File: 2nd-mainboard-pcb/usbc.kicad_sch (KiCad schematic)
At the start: 13 parts, among them J1 USB_C_Receptacle, U2 PTS647SM38SMTR2LFS, U5 FT232RL

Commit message: verpolungsschutz und powerin
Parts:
- renumbered R1 to R21
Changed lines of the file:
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@@
 		(dnp no)
 		(fields_autoplaced yes)
-		(property "Reference" "R1"
+		(property "Reference" "R21"
 			(at 86.36 67.3099 0)
 			(effects
@@
 			(project "2nd-mainboard-pcb"
 				(path "/6926a609-8b92-4b3a-88c8-3d023174b977/c1b5568e-d56d-48b3-9b9c-ea1ab28283d3"
-					(reference "R1")
+					(reference "R21")
 					(unit 1)
 				)

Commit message: finished stacked design, annotaded
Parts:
- removed D1: SMAJ5.0A, Diode_SMD:D_SMA, symbol Diode:SMAJ5.0A
- added C15: 10µF, symbol Device:C
- added C16: 100nF, symbol Device:C
- added D2: WE-TVSP_DO-214AA_600W_BI, WE-TVSP_DO-214AA_600W_BI:WE-TVSP_DO-214AA_BIDIRECTIONAL, symbol Imported_Component_Symbols:WE-TVSP_DO-214AA_600W_BI
- U5: renamed from U2; footprint SW_PTS647SM38SMTR2LFS_CNK -> Imported_Component_Footprints:SW_PTS647SM38SMTR2LFS_CNK
- renumbered C1 to C14, C2 to C17, C4 to C18, D2 to D3, J1 to J2, R2 to R10, R3 to R11, R4 to R12, R5 to R13, R21 to R9, U5 to U6
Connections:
- net +5V: no longer C18.1, J2.A4 (VBUS), J2.A9 (VBUS), J2.B4 (VBUS), J2.B9 (VBUS), R11.1, U6.20 (VCC), U6.4 (VCCIO)
- net GND: now also U6.25 (AGND), C15.2, C16.2, D2.1
- new net +5V_POW: R11.1, U6.4 (VCCIO)
- new net +5V_USBC: C15.1, C16.1, C18.1, D2.2, J2.A4 (VBUS), J2.A9 (VBUS), J2.B4 (VBUS), J2.B9 (VBUS), U6.20 (VCC)
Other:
- moved on the sheet: C14, C17, C18, D3, J2, R10, R11, R12, R13, R9, U5, U6

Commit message: alle bauteile hinzugefügt
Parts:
- removed D3: LED, symbol Device:LED
- removed J2: USB_C_Receptacle, Connector_USB:USB_C_Receptacle_GCT_USB4085, symbol Connector:USB_C_Receptacle
- removed R12, R13: 10k, symbol Device:R
- added P1: USB_C_Plug_USB2.0, Connector_USB:USB_C_Receptacle_GCT_USB4085, symbol Connector:USB_C_Plug_USB2.0
- C15: footprint (none) -> Capacitor_SMD:C_0805_2012Metric_Pad1.18x1.45mm_HandSolder
- C16: footprint (none) -> Capacitor_SMD:C_0402_1005Metric_Pad0.74x0.62mm_HandSolder
- C17: renamed from C18; footprint (none) -> Capacitor_SMD:C_0402_1005Metric_Pad0.74x0.62mm_HandSolder
- C18: renamed from C17; footprint (none) -> Capacitor_SMD:C_0402_1005Metric_Pad0.74x0.62mm_HandSolder
- C19: renamed from C14; footprint (none) -> Capacitor_SMD:C_0805_2012Metric_Pad1.18x1.45mm_HandSolder
- D2: footprint WE-TVSP_DO-214AA_600W_BI:WE-TVSP_DO-214AA_BIDIRECTIONAL -> Imported_Component_Footprints:824521241
- R10, R11, R9: footprint (none) -> Resistor_SMD:R_0402_1005Metric
- renumbered U6 to U5, U5 to U6
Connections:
- net +5V_USBC: now also P1.A4 (VBUS), P1.A9 (VBUS), P1.B4 (VBUS), P1.B9 (VBUS)
- net GND: now also P1.A1 (GND), P1.A12 (GND), P1.B1 (GND), P1.B12 (GND)
- net USBD+: now also P1.A6 (D+)
- net USBD-: now also P1.A7 (D-)
- net at R9.1: now also P1.B5 (VCONN)
- net at C19.1: now also P1.S1 (SHIELD)
- net at R10.1: now also P1.A5 (CC)
- no-connect marks 23 -> 16
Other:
- moved on the sheet: C19

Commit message: mehr positioning
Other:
- moved on the sheet: C17, C18, R11, U5, U6

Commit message: Fan-PCB-Beginning
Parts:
- removed C18: 100nF, Capacitor_SMD:C_0402_1005Metric_Pad0.74x0.62mm_HandSolder, symbol Device:C
- renumbered C19 to C18
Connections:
- net +3V3: no longer names the net of U5.17 (3V3OUT)
- no-connect marks 16 -> 18
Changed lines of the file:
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@@
-	)
-	(junction
-		(at 132.08 62.23)
-		(diameter 0)
-		(color 0 0 0 0)
 	)
 	(junction
@@
 	)
 	(no_connect
+		(at 149.86 53.34)
+	)
+	(no_connect
+		(at 156.21 62.23)
+	)
+	(no_connect
 		(at 196.85 97.79)
 	)
@@
 	(wire
 		(pts
-			(xy 132.08 69.85) (xy 132.08 73.66)
-		)
-		(stroke
-			(width 0)
-			(type default)
-		)
-	)
-	(wire
-		(pts
 			(xy 57.15 20.32) (xy 64.77 20.32)
 		)
@@
 	(wire
 		(pts
-			(xy 132.08 62.23) (xy 156.21 62.23)
-		)
-		(stroke
-			(width 0)
-			(type default)
-		)
-	)
-	(wire
-		(pts
 			(xy 109.22 36.83) (xy 109.22 31.75)
 		)
@@
 		(pts
 			(xy 152.4 80.01) (xy 156.21 80.01)
-		)
-		(stroke
-			(width 0)
-			(type default)
-		)
-	)
-	(wire
-		(pts
-			(xy 132.08 59.69) (xy 132.08 62.23)
 		)
 		(stroke
@@
 		(dnp no)
 		(fields_autoplaced yes)
-		(property "Reference" "#PWR026"
+		(property "Reference" "#PWR027"
 			(at 62.23 63.5 0)
 			(effects
@@
 			(project "2nd-mainboard-pcb"
 				(path "/6926a609-8b92-4b3a-88c8-3d023174b977/c1b5568e-d56d-48b3-9b9c-ea1ab28283d3"
-					(reference "#PWR026")
+					(reference "#PWR027")
 					(unit 1)
 				)
@@
 		(dnp no)
 		(fields_autoplaced yes)
-		(property "Reference" "#PWR024"
+		(property "Reference" "#PWR023"
 			(at 179.07 39.37 0)
 			(effects
@@
 			(project "2nd-mainboard-pcb"
 				(path "/6926a609-8b92-4b3a-88c8-3d023174b977/c1b5568e-d56d-48b3-9b9c-ea1ab28283d3"
-					(reference "#PWR024")
+					(reference "#PWR023")
 					(unit 1)
 				)
@@
 		(dnp no)
 		(fields_autoplaced yes)
-		(property "Reference" "C19"
+		(property "Reference" "C18"
 			(at 26.67 78.7399 0)
 			(effects
@@
 			(project "2nd-mainboard-pcb"
 				(path "/6926a609-8b92-4b3a-88c8-3d023174b977/c1b5568e-d56d-48b3-9b9c-ea1ab28283d3"
-					(reference "C19")
+					(reference "C18")
 					(unit 1)
 				)
@@
 		(dnp no)
 		(fields_autoplaced yes)
-		(property "Reference" "#PWR027"
+		(property "Reference" "#PWR028"
 			(at 71.12 63.5 0)
 			(effects
@@
 			(project "2nd-mainboard-pcb"
 				(path "/6926a609-8b92-4b3a-88c8-3d023174b977/c1b5568e-d56d-48b3-9b9c-ea1ab28283d3"
-					(reference "#PWR027")
+					(reference "#PWR028")
 					(unit 1)
 				)
@@
 		(dnp no)
 		(fields_autoplaced yes)
-		(property "Reference" "#PWR035"
+		(property "Reference" "#PWR033"
 			(at 50.8 125.73 0)
 			(effects
@@
 			(project "2nd-mainboard-pcb"
 				(path "/6926a609-8b92-4b3a-88c8-3d023174b977/c1b5568e-d56d-48b3-9b9c-ea1ab28283d3"
-					(reference "#PWR035")
-					(unit 1)
-				)
-			)
-		)
-	)
-	(symbol
-		(lib_id "power:GND")
-		(at 132.08 73.66 0)
-		(unit 1)
-		(exclude_from_sim no)
-		(in_bom yes)
-		(on_board yes)
-		(dnp no)
-		(fields_autoplaced yes)
-		(property "Reference" "#PWR031"
-			(at 132.08 80.01 0)
-			(effects
-				(font
-					(size 1.27 1.27)
-				)
-				(hide yes)
-			)
-		)
-		(property "Value" "GND"
-			(at 132.08 78.74 0)
-			(effects
-				(font
-					(size 1.27 1.27)
-				)
-			)
-		)
-		(property "Footprint" ""
-			(at 132.08 73.66 0)
-			(effects
-				(font
-					(size 1.27 1.27)
-				)
-				(hide yes)
-			)
-		)
-		(property "Datasheet" ""
-			(at 132.08 73.66 0)
-			(effects
-				(font
-					(size 1.27 1.27)
-				)
-				(hide yes)
-			)
-		)
-		(property "Description" "Power symbol creates a global label with name \"GND\" , ground"
-			(at 132.08 73.66 0)
-			(effects
-				(font
-					(size 1.27 1.27)
-				)
-				(hide yes)
-			)
-		)
-		(pin "1"
-		)
-		(instances
-			(project "2nd-mainboard-pcb"
-				(path "/6926a609-8b92-4b3a-88c8-3d023174b977/c1b5568e-d56d-48b3-9b9c-ea1ab28283d3"
-					(reference "#PWR031")
+					(reference "#PWR033")
 					(unit 1)
 				)
@@
 		(on_board yes)
 		(dnp no)
-		(property "Reference" "#PWR034"
+		(property "Reference" "#PWR031"
 			(at 114.3 106.68 0)
 			(effects
@@
 			(project "2nd-mainboard-pcb"
 				(path "/6926a609-8b92-4b3a-88c8-3d023174b977/c1b5568e-d56d-48b3-9b9c-ea1ab28283d3"
-					(reference "#PWR034")
+					(reference "#PWR031")
 					(unit 1)
 				)
@@
 	)
 	(symbol
-		(lib_id "Device:C")
-		(at 132.08 66.04 0)
-		(unit 1)
-		(exclude_from_sim no)
-		(in_bom yes)
-		(on_board yes)
-		(dnp no)
-		(fields_autoplaced yes)
-		(property "Reference" "C18"
-			(at 135.89 64.7699 0)
-			(effects
-				(font
-					(size 1.27 1.27)
-				)
-				(justify left)
-			)
-		)
-		(property "Value" "100nF"
-			(at 135.89 67.3099 0)
-			(effects
-				(font
-					(size 1.27 1.27)
-				)
-				(justify left)
-			)
-		)
-		(property "Footprint" "Capacitor_SMD:C_0402_1005Metric_Pad0.74x0.62mm_HandSolder"
-			(at 133.0452 69.85 0)
-			(effects
-				(font
-					(size 1.27 1.27)
-				)
-				(hide yes)
-			)
-		)
-		(property "Datasheet" "~"
-			(at 132.08 66.04 0)
-			(effects
-				(font
-					(size 1.27 1.27)
-				)
-				(hide yes)
-			)
-		)
-		(property "Description" "Unpolarized capacitor"
-			(at 132.08 66.04 0)
-			(effects
-				(font
-					(size 1.27 1.27)
-				)
-				(hide yes)
-			)
-		)
-		(pin "1"
-		)
-		(pin "2"
-		)
-		(instances
-			(project "2nd-mainboard-pcb"
-				(path "/6926a609-8b92-4b3a-88c8-3d023174b977/c1b5568e-d56d-48b3-9b9c-ea1ab28283d3"
-					(reference "C18")
-					(unit 1)
-				)
-			)
-		)
-	)
-	(symbol
 		(lib_id "power:GND")
 		(at 193.04 50.8 0)
@@
 		(dnp no)
 		(fields_autoplaced yes)
-		(property "Reference" "#PWR028"
+		(property "Reference" "#PWR026"
 			(at 193.04 57.15 0)
 			(effects
@@
 			(project "2nd-mainboard-pcb"
 				(path "/6926a609-8b92-4b3a-88c8-3d023174b977/c1b5568e-d56d-48b3-9b9c-ea1ab28283d3"
-					(reference "#PWR028")
+					(reference "#PWR026")
 					(unit 1)
 				)
@@
 		(dnp no)
 		(fields_autoplaced yes)
-		(property "Reference" "#PWR030"
+		(property "Reference" "#PWR029"
 			(at 30.48 87.63 0)
 			(effects
@@
 			(project "2nd-mainboard-pcb"
 				(path "/6926a609-8b92-4b3a-88c8-3d023174b977/c1b5568e-d56d-48b3-9b9c-ea1ab28283d3"
-					(reference "#PWR030")
+					(reference "#PWR029")
 					(unit 1)
 				)
@@
 		(dnp no)
 		(fields_autoplaced yes)
-		(property "Reference" "#PWR032"
+		(property "Reference" "#PWR030"
 			(at 22.86 95.25 0)
 			(effects
@@
 			(project "2nd-mainboard-pcb"
 				(path "/6926a609-8b92-4b3a-88c8-3d023174b977/c1b5568e-d56d-48b3-9b9c-ea1ab28283d3"
-					(reference "#PWR032")
+					(reference "#PWR030")
 					(unit 1)
 				)
@@
 		(dnp no)
 		(fields_autoplaced yes)
-		(property "Reference" "#PWR033"
+		(property "Reference" "#PWR032"
 			(at 181.61 116.84 0)
 			(effects
@@
 			(project "2nd-mainboard-pcb"
 				(path "/6926a609-8b92-4b3a-88c8-3d023174b977/c1b5568e-d56d-48b3-9b9c-ea1ab28283d3"
-					(reference "#PWR033")
+					(reference "#PWR032")
 					(unit 1)
 				)
@@
 	)
 	(symbol
-		(lib_id "power:+3V3")
-		(at 132.08 59.69 0)
-		(unit 1)
-		(exclude_from_sim no)
-		(in_bom yes)
-		(on_board yes)
-		(dnp no)
-		(fields_autoplaced yes)
-		(property "Reference" "#PWR029"
-			(at 132.08 63.5 0)
-			(effects
-				(font
-					(size 1.27 1.27)
-				)
-				(hide yes)
-			)
-		)
-		(property "Value" "+3V3"
-			(at 132.08 54.61 0)
-			(effects
-				(font
-					(size 1.27 1.27)
-				)
-			)
-		)
-		(property "Footprint" ""
-			(at 132.08 59.69 0)
-			(effects
-				(font
-					(size 1.27 1.27)
-				)
-				(hide yes)
-			)
-		)
-		(property "Datasheet" ""
-			(at 132.08 59.69 0)
-			(effects
-				(font
-					(size 1.27 1.27)
-				)
-				(hide yes)
-			)
-		)
-		(property "Description" "Power symbol creates a global label with name \"+3V3\""
-			(at 132.08 59.69 0)
-			(effects
-				(font
-					(size 1.27 1.27)
-				)
-				(hide yes)
-			)
-		)
-		(pin "1"
-		)
-		(instances
-			(project "2nd-mainboard-pcb"
-				(path "/6926a609-8b92-4b3a-88c8-3d023174b977/c1b5568e-d56d-48b3-9b9c-ea1ab28283d3"
-					(reference "#PWR029")
-					(unit 1)
-				)
-			)
-		)
-	)
-	(symbol
 		(lib_id "power:GND")
 		(at 95.25 40.64 0)
@@
 		(dnp no)
 		(fields_autoplaced yes)
-		(property "Reference" "#PWR023"
+		(property "Reference" "#PWR024"
 			(at 95.25 46.99 0)
 			(effects
@@
 			(project "2nd-mainboard-pcb"
 				(path "/6926a609-8b92-4b3a-88c8-3d023174b977/c1b5568e-d56d-48b3-9b9c-ea1ab28283d3"
-					(reference "#PWR023")
+					(reference "#PWR024")
 					(unit 1)
 				)

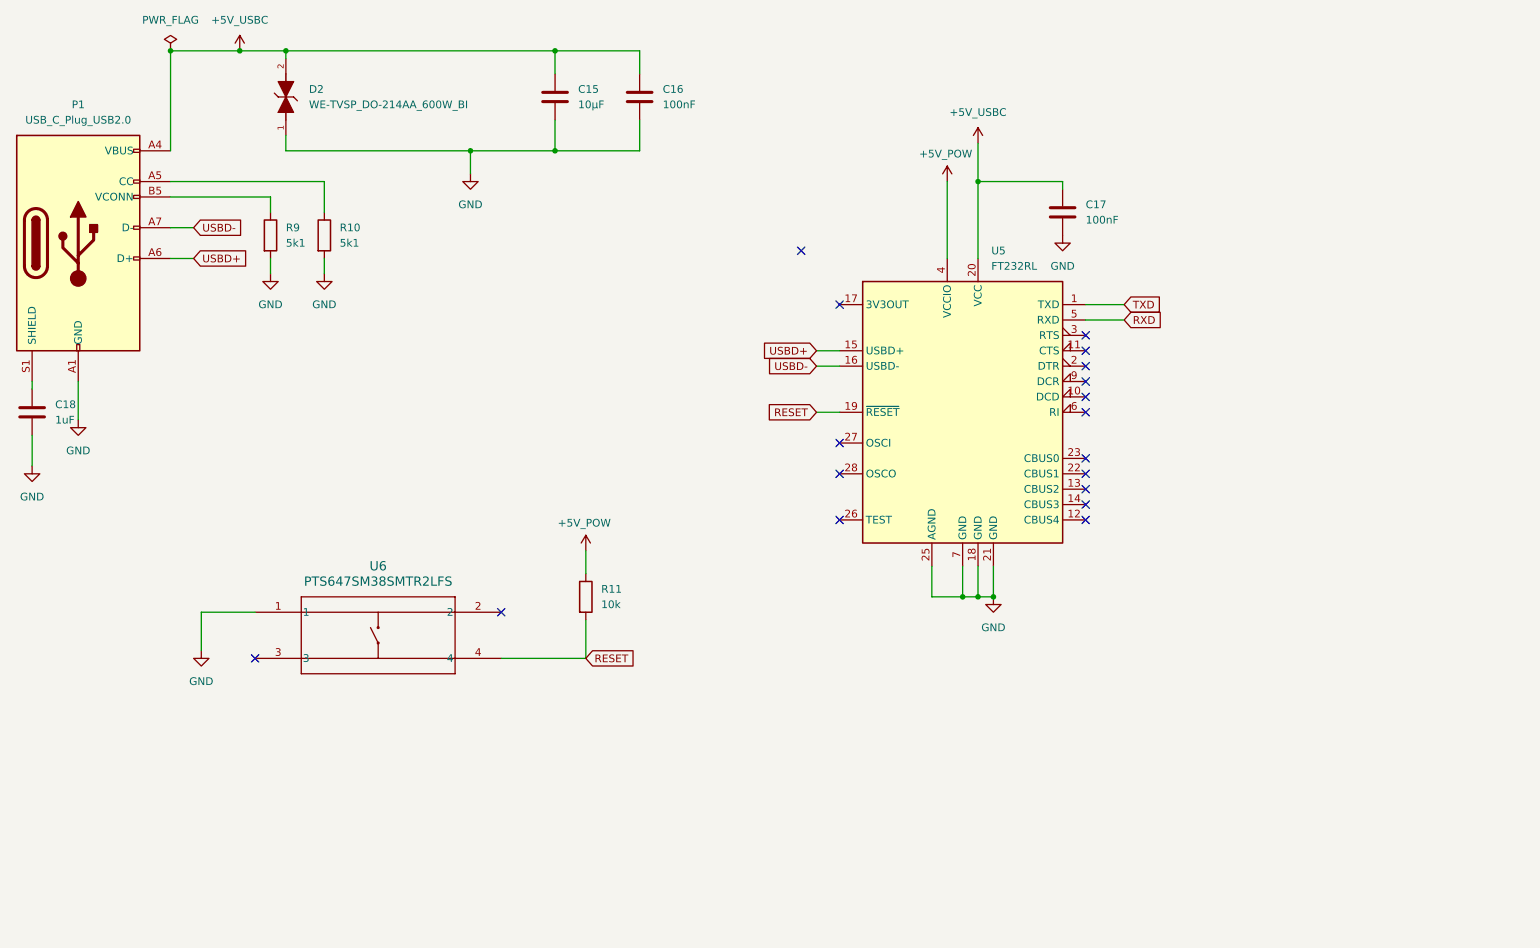
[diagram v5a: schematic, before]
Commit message: updated a bit of the track widths, removed comments in schematic
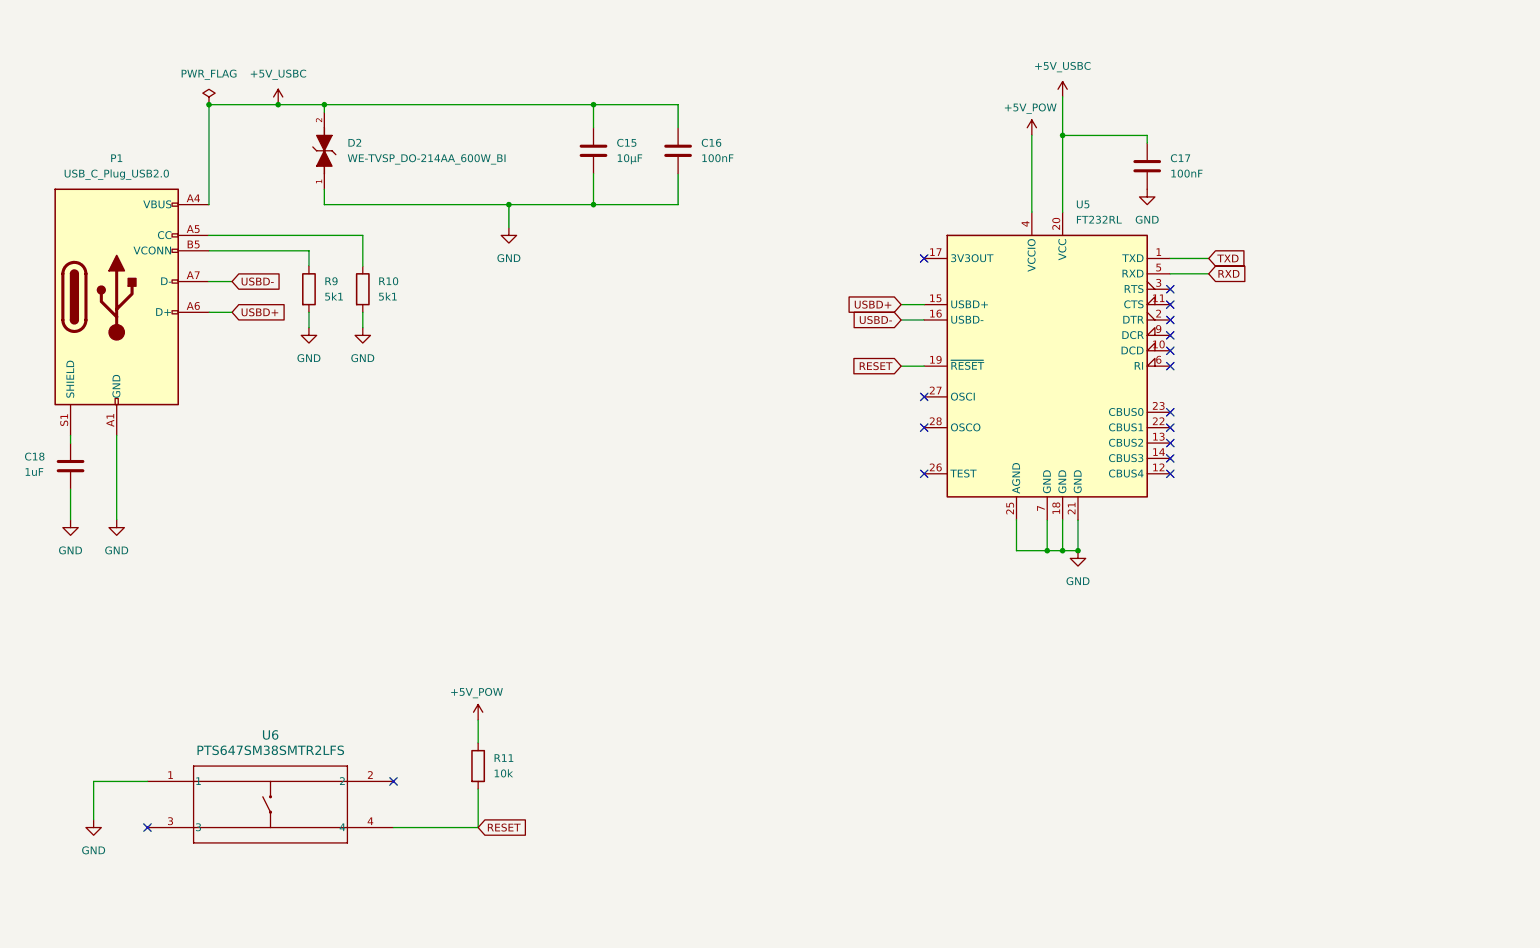
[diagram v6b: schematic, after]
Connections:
- no-connect marks 18 -> 17
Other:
- moved on the sheet: C15, C16, C17, C18, D2, P1, R10, R11, R9, U5, U6

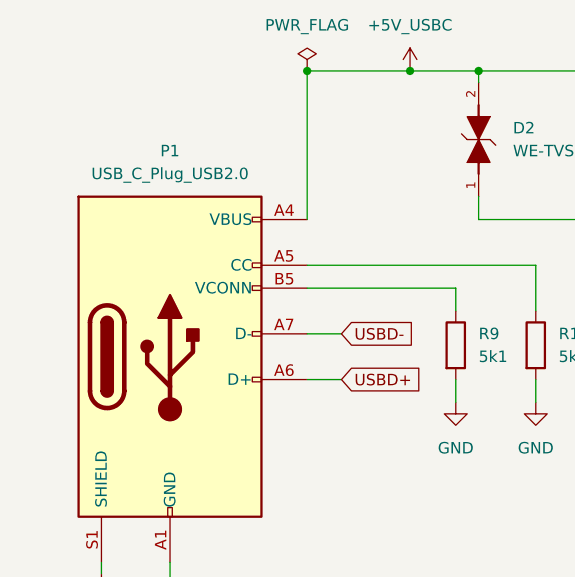
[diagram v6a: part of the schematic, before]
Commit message: further configured wireviz, editet excel
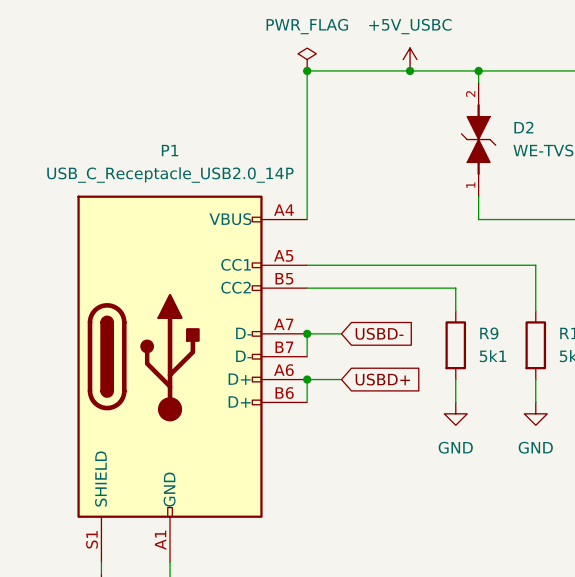
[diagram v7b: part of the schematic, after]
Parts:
- removed P1: USB_C_Plug_USB2.0, Connector_USB:USB_C_Receptacle_GCT_USB4085, symbol Connector:USB_C_Plug_USB2.0
- added P1: USB_C_Receptacle_USB2.0_14P, Connector_USB:USB_C_Receptacle_GCT_USB4085, symbol Connector:USB_C_Receptacle_USB2.0_14P
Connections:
- net +5V_USBC: now also P1.A4 (VBUS), P1.A9 (VBUS), P1.B4 (VBUS), P1.B9 (VBUS)
- net GND: now also P1.A1 (GND), P1.A12 (GND), P1.B1 (GND), P1.B12 (GND)
- net USBD+: now also P1.A6 (D+), P1.B6 (D+)
- net USBD-: now also P1.A7 (D-), P1.B7 (D-)
- net at R10.1: now also P1.A5 (CC1)
- net at R9.1: now also P1.B5 (CC2)
- net at C18.1: now also P1.S1 (SHIELD)
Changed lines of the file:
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@@
+	)
+	(junction
+		(at 52.07 58.42)
+		(diameter 0)
+		(color 0 0 0 0)
 	)
 	(junction
@@
 	)
 	(junction
+		(at 52.07 63.5)
+		(diameter 0)
+		(color 0 0 0 0)
+	)
+	(junction
 		(at 71.12 29.21)
 		(diameter 0)
@@
 	(wire
 		(pts
+			(xy 52.07 63.5) (xy 52.07 66.04)
+		)
+		(stroke
+			(width 0)
+			(type default)
+		)
+	)
+	(wire
+		(pts
 			(xy 96.52 130.81) (xy 96.52 134.62)
 		)
@@
 		(pts
 			(xy 129.54 40.64) (xy 129.54 45.72)
+		)
+		(stroke
+			(width 0)
+			(type default)
+		)
+	)
+	(wire
+		(pts
+			(xy 52.07 58.42) (xy 52.07 60.96)
 		)
 		(stroke
@@
 	)
 	(symbol
-		(lib_id "Connector:USB_C_Plug_USB2.0")
-		(at 36.83 60.96 0)
-		(unit 1)
-		(exclude_from_sim no)
-		(in_bom yes)
-		(on_board yes)
-		(dnp no)
-		(fields_autoplaced yes)
-		(property "Reference" "P1"
-			(at 36.83 38.1 0)
-			(effects
-				(font
-					(size 1.27 1.27)
-				)
-			)
-		)
-		(property "Value" "USB_C_Plug_USB2.0"
-			(at 36.83 40.64 0)
-			(effects
-				(font
-					(size 1.27 1.27)
-				)
-			)
-		)
-		(property "Footprint" "Connector_USB:USB_C_Receptacle_GCT_USB4085"
-			(at 40.64 60.96 0)
-			(effects
-				(font
-					(size 1.27 1.27)
-				)
-				(hide yes)
-			)
-		)
-		(property "Datasheet" "https://www.usb.org/sites/default/files/documents/usb_type-c.zip"
-			(at 40.64 60.96 0)
-			(effects
-				(font
-					(size 1.27 1.27)
-				)
-				(hide yes)
-			)
-		)
-		(property "Description" "USB 2.0-only Type-C Plug connector"
-			(at 36.83 60.96 0)
-			(effects
-				(font
-					(size 1.27 1.27)
-				)
-				(hide yes)
-			)
-		)
-		(pin "B5"
-		)
-		(pin "B9"
-		)
-		(pin "A9"
-		)
-		(pin "B12"
-		)
-		(pin "B1"
-		)
-		(pin "A12"
-		)
-		(pin "A5"
-		)
-		(pin "A4"
-		)
-		(pin "A1"
-		)
-		(pin "B4"
-		)
-		(pin "A7"
-		)
-		(pin "S1"
-		)
-		(pin "A6"
-		)
-		(instances
-			(project ""
-				(path "/6926a609-8b92-4b3a-88c8-3d023174b977/c1b5568e-d56d-48b3-9b9c-ea1ab28283d3"
-					(reference "P1")
-					(unit 1)
-				)
-			)
-		)
-	)
-	(symbol
 		(lib_id "Device:C")
 		(at 207.01 39.37 0)
@@
 					(unit 1)
 				)
+			)
+		)
+	)
+	(symbol
+		(lib_id "Connector:USB_C_Receptacle_USB2.0_14P")
+		(at 36.83 60.96 0)
+		(unit 1)
+		(exclude_from_sim no)
+		(in_bom yes)
+		(on_board yes)
+		(dnp no)
+		(fields_autoplaced yes)
+		(property "Reference" "P1"
+			(at 36.83 38.1 0)
+			(effects
+				(font
+					(size 1.27 1.27)
+				)
+			)
+		)
+		(property "Value" "USB_C_Receptacle_USB2.0_14P"
+			(at 36.83 40.64 0)
+			(effects
+				(font
+					(size 1.27 1.27)
+				)
+			)
+		)
+		(property "Footprint" "Connector_USB:USB_C_Receptacle_GCT_USB4085"
+			(at 40.64 60.96 0)
+			(effects
+				(font
+					(size 1.27 1.27)
+				)
+				(hide yes)
+			)
+		)
+		(property "Datasheet" "https://www.usb.org/sites/default/files/documents/usb_type-c.zip"
+			(at 40.64 60.96 0)
+			(effects
+				(font
+					(size 1.27 1.27)
+				)
+				(hide yes)
+			)
+		)
+		(property "Description" "USB 2.0-only 14P Type-C Receptacle connector"
+			(at 36.83 60.96 0)
+			(effects
+				(font
+					(size 1.27 1.27)
+				)
+				(hide yes)
+			)
+		)
+		(pin "A5"
+		)
+		(pin "B5"
+		)
+		(pin "A4"
+		)
+		(pin "B9"
+		)
+		(pin "B7"
+		)
+		(pin "S1"
+		)
+		(pin "B6"
+		)
+		(pin "B12"
+		)
+		(pin "A12"
+		)
+		(pin "A6"
+		)
+		(pin "B4"
+		)
+		(pin "A7"
+		)
+		(pin "A9"
+		)
+		(pin "B1"
+		)
+		(pin "A1"
+		)
+		(instances
+			(project ""
+				(path "/6926a609-8b92-4b3a-88c8-3d023174b977/c1b5568e-d56d-48b3-9b9c-ea1ab28283d3"
+					(reference "P1")
+					(unit 1)
+				)
